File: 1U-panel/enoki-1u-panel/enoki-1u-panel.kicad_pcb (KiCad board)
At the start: 2 copper layers, 40.6 x 39.6 mm, 3 parts, among them J1 EuroPi Header, J2 Monome Header

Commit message: save
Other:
- outline, holes or cut-outs redrawn
- board text added: "Enoki!"
- board text added: "Toadstool Tech"
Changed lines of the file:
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@@
         (effects (font (size 1 1) (thickness 0.15)))
     )
-    (fp_text user "3V3" (at 8.636 -1.397 45 unlocked) (layer "F.SilkS")
-        (effects (font (size 0.75 0.75) (thickness 0.1)) (justify left bottom))
-    )
-    (fp_text user "RST" (at -1.524 -1.397 45 unlocked) (layer "F.SilkS")
+    (fp_text user "GND" (at 6.096 -1.397 45 unlocked) (layer "F.SilkS")
+        (effects (font (size 0.75 0.75) (thickness 0.1)) (justify left bottom))
+    )
+    (fp_text user "CS" (at -6.604 -1.397 45 unlocked) (layer "F.SilkS")
         (effects (font (size 0.75 0.75) (thickness 0.1)) (justify left bottom))
     )
@@
         (effects (font (size 1.09 1.09) (thickness 0.15)))
     )
+    (fp_text user "SDA" (at 1.016 -1.397 45 unlocked) (layer "F.SilkS")
+        (effects (font (size 0.75 0.75) (thickness 0.1)) (justify left bottom))
+    )
+    (fp_text user "RST" (at -1.524 -1.397 45 unlocked) (layer "F.SilkS")
+        (effects (font (size 0.75 0.75) (thickness 0.1)) (justify left bottom))
+    )
     (fp_text user "DC" (at -4.064 -1.397 45 unlocked) (layer "F.SilkS")
         (effects (font (size 0.75 0.75) (thickness 0.1)) (justify left bottom))
@@
         (effects (font (size 0.75 0.75) (thickness 0.1)) (justify left bottom))
     )
-    (fp_text user "CS" (at -6.604 -1.397 45 unlocked) (layer "F.SilkS")
-        (effects (font (size 0.75 0.75) (thickness 0.1)) (justify left bottom))
-    )
-    (fp_text user "GND" (at 6.096 -1.397 45 unlocked) (layer "F.SilkS")
-        (effects (font (size 0.75 0.75) (thickness 0.1)) (justify left bottom))
-    )
-    (fp_text user "SDA" (at 1.016 -1.397 45 unlocked) (layer "F.SilkS")
+    (fp_text user "3V3" (at 8.636 -1.397 45 unlocked) (layer "F.SilkS")
         (effects (font (size 0.75 0.75) (thickness 0.1)) (justify left bottom))
     )
@@
     (pad "x" thru_hole circle (at 16.51 15.24) (size 1.524 1.524) (drill 0.762) (layers "*.Cu" "*.Mask"))
     (pad "x" thru_hole circle (at 16.51 17.78) (size 1.524 1.524) (drill 0.762) (layers "*.Cu" "*.Mask"))
+    (model "${KICAD7_3RD_PARTY}/Allen-Synthesis-KiCad-Library/3dmodels/toadstool-tech-enoki-oled.wrl"
+      (offset (xyz 19 2.5 4))
+      (scale (xyz 0.394 0.394 0.394))
+      (rotate (xyz 0 180 0))
+    )
   )
   (footprint "Connector_IDC:IDC-Header_2x03_P2.54mm_Vertical" (layer "B.Cu")
@@
   (gr_rect (start 0 0) (end 40.64 39.65)
     (stroke (width 0.1) (type default)) (fill none) (layer "Edge.Cuts"))
+  (gr_arc (start 4.630004 2.999999) (mid 5.098634 1.86863) (end 6.230004 1.400002)
+    (stroke (width 0.15) (type default)) (layer "Edge.Cuts"))
+  (gr_arc (start 6.230002 4.599997) (mid 5.098633 4.131367) (end 4.630005 2.999997)
+    (stroke (width 0.15) (type default)) (layer "Edge.Cuts"))
+  (gr_line (start 6.23 1.4) (end 8.77 1.4)
+    (stroke (width 0.15) (type default)) (layer "Edge.Cuts"))
+  (gr_arc (start 4.630004 36.649999) (mid 5.098634 35.51863) (end 6.230004 35.050002)
+    (stroke (width 0.15) (type default)) (layer "Edge.Cuts"))
+  (gr_arc (start 8.769998 1.400003) (mid 9.901367 1.868633) (end 10.369995 3.000003)
+    (stroke (width 0.15) (type default)) (layer "Edge.Cuts"))
+  (gr_line (start 6.23 4.6) (end 8.77 4.6)
+    (stroke (width 0.15) (type default)) (layer "Edge.Cuts"))
+  (gr_arc (start 8.769999 35.05) (mid 9.901368 35.51863) (end 10.369996 36.65)
+    (stroke (width 0.15) (type default)) (layer "Edge.Cuts"))
+  (gr_arc (start 10.369996 3.000001) (mid 9.901366 4.13137) (end 8.769996 4.599998)
+    (stroke (width 0.15) (type default)) (layer "Edge.Cuts"))
+  (gr_arc (start 10.37 36.65) (mid 9.90137 37.781369) (end 8.77 38.249997)
+    (stroke (width 0.15) (type default)) (layer "Edge.Cuts"))
+  (gr_arc (start 6.230002 38.249997) (mid 5.098633 37.781367) (end 4.630005 36.649997)
+    (stroke (width 0.15) (type default)) (layer "Edge.Cuts"))
+  (gr_line (start 6.23 35.05) (end 8.77 35.05)
+    (stroke (width 0.15) (type default)) (layer "Edge.Cuts"))
+  (gr_line (start 6.23 38.25) (end 8.77 38.25)
+    (stroke (width 0.15) (type default)) (layer "Edge.Cuts"))
   (gr_text "GND" (at 25.908 9.652 45) (layer "B.SilkS")
     (effects (font (size 0.75 0.75) (thickness 0.1)) (justify right mirror))
@@
     (effects (font (size 0.75 0.75) (thickness 0.1)) (justify right mirror))
   )
+  (gr_text "Enoki!" (at 39.37 3) (layer "F.SilkS")
+    (effects (font (size 1.5 1.5) (thickness 0.3)) (justify right))
+  )
+  (gr_text "Toadstool Tech" (at 39.37 36.65) (layer "F.SilkS")
+    (effects (font (size 1.5 1.5) (thickness 0.3)) (justify right))
+  )
 )

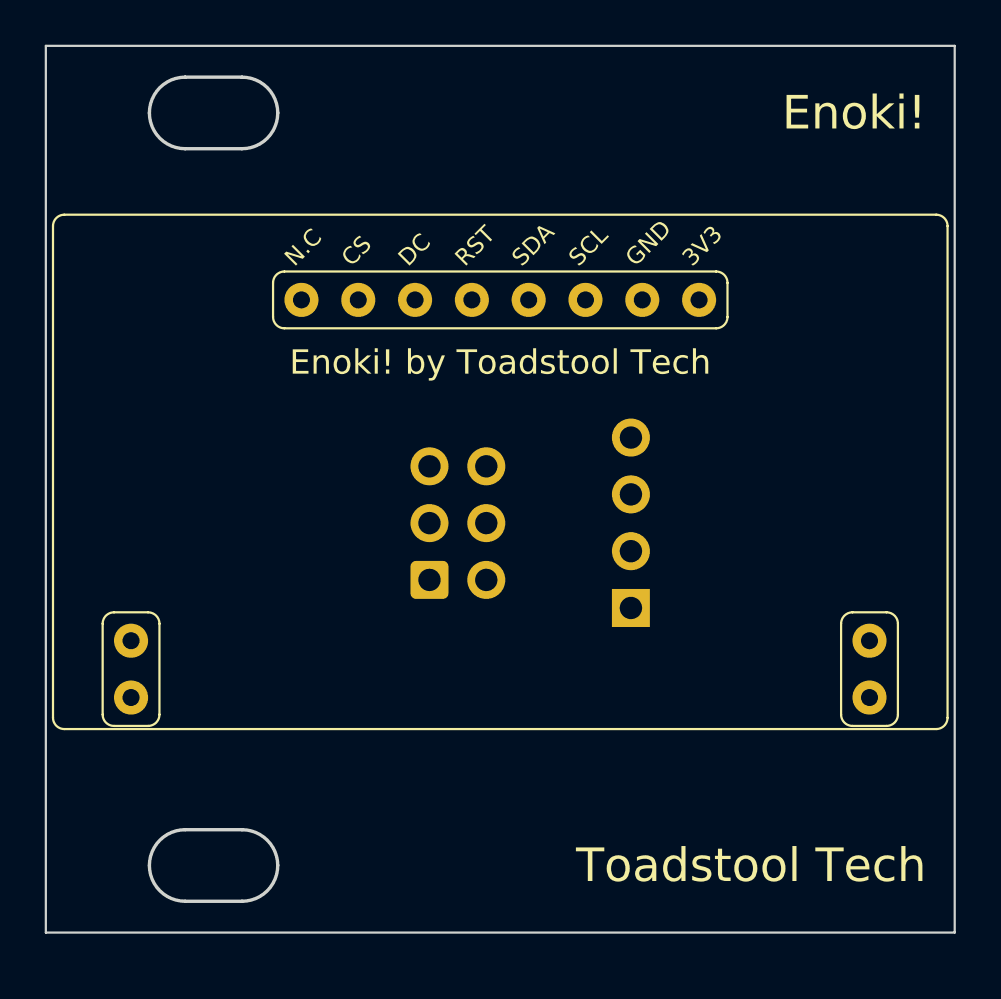
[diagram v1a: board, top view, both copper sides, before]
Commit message: route 1u panel
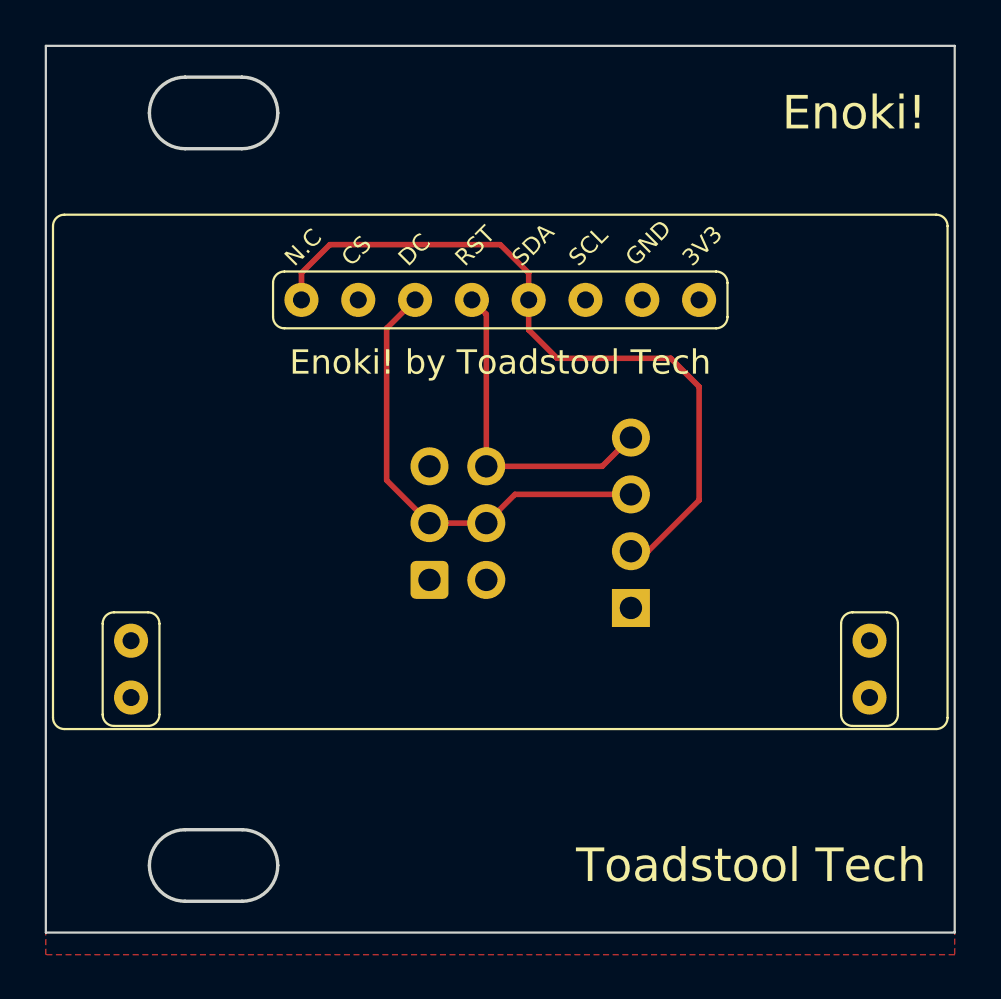
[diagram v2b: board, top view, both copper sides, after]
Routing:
- net +3V3: track 0.00 -> 32.7 mm
- net /SCL: track 0.00 -> 20.8 mm
- net /SDA: track 0.00 -> 14.7 mm
- added copper zone on F.Cu, net GND
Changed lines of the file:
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@@
     (effects (font (size 1.5 1.5) (thickness 0.3)) (justify right))
   )
+  (segment (start 29.21 20.32) (end 26.934 22.596) (width 0.25) (layer "F.Cu") (net 1))
+  (segment (start 21.59 12.7) (end 22.86 13.97) (width 0.25) (layer "F.Cu") (net 1))
+  (segment (start 26.934 22.596) (end 26.162 22.596) (width 0.25) (layer "F.Cu") (net 1))
+  (segment (start 21.59 10.16) (end 20.32 8.89) (width 0.25) (layer "F.Cu") (net 1))
+  (segment (start 21.59 11.36) (end 21.59 12.7) (width 0.25) (layer "F.Cu") (net 1))
+  (segment (start 21.59 11.36) (end 21.59 10.16) (width 0.25) (layer "F.Cu") (net 1))
+  (segment (start 11.43 10.16) (end 11.43 11.36) (width 0.25) (layer "F.Cu") (net 1))
+  (segment (start 22.86 13.97) (end 27.94 13.97) (width 0.25) (layer "F.Cu") (net 1))
+  (segment (start 29.21 15.24) (end 29.21 20.32) (width 0.25) (layer "F.Cu") (net 1))
+  (segment (start 27.94 13.97) (end 29.21 15.24) (width 0.25) (layer "F.Cu") (net 1))
+  (segment (start 20.32 8.89) (end 12.7 8.89) (width 0.25) (layer "F.Cu") (net 1))
+  (segment (start 12.7 8.89) (end 11.43 10.16) (width 0.25) (layer "F.Cu") (net 1))
+  (segment (start 26.162 20.056) (end 20.9795 20.056) (width 0.25) (layer "F.Cu") (net 3))
+  (segment (start 17.1545 21.341) (end 19.6945 21.341) (width 0.25) (layer "F.Cu") (net 3))
+  (segment (start 16.51 11.36) (end 15.24 12.63) (width 0.25) (layer "F.Cu") (net 3))
+  (segment (start 20.9795 20.056) (end 19.6945 21.341) (width 0.25) (layer "F.Cu") (net 3))
+  (segment (start 15.24 19.4265) (end 17.1545 21.341) (width 0.25) (layer "F.Cu") (net 3))
+  (segment (start 15.24 12.63) (end 15.24 19.4265) (width 0.25) (layer "F.Cu") (net 3))
+  (segment (start 24.877 18.801) (end 19.6945 18.801) (width 0.25) (layer "F.Cu") (net 4))
+  (segment (start 26.162 17.516) (end 24.877 18.801) (width 0.25) (layer "F.Cu") (net 4))
+  (segment (start 19.6945 18.801) (end 19.6945 12.0045) (width 0.25) (layer "F.Cu") (net 4))
+  (segment (start 19.6945 12.0045) (end 19.05 11.36) (width 0.25) (layer "F.Cu") (net 4))
+  (zone (net 2) (net_name "GND") (layer "F.Cu") (hatch edge 0.5)
+    (connect_pads (clearance 0.5))
+    (min_thickness 0.25) (filled_areas_thickness no)
+    (fill yes (thermal_gap 0.5) (thermal_bridge_width 0.5))
+    (polygon
+      (pts
+        (xy 0 0)
+        (xy 40.64 0)
+        (xy 40.64 40.64)
+        (xy 0 40.64)
+      )
+    )
+  )
 )
